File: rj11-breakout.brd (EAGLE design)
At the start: 100 x 80 mm, 2 parts, among them J1 22-27-2061-06, X1 XRJK-S-01-6-6-0-2G2-NO

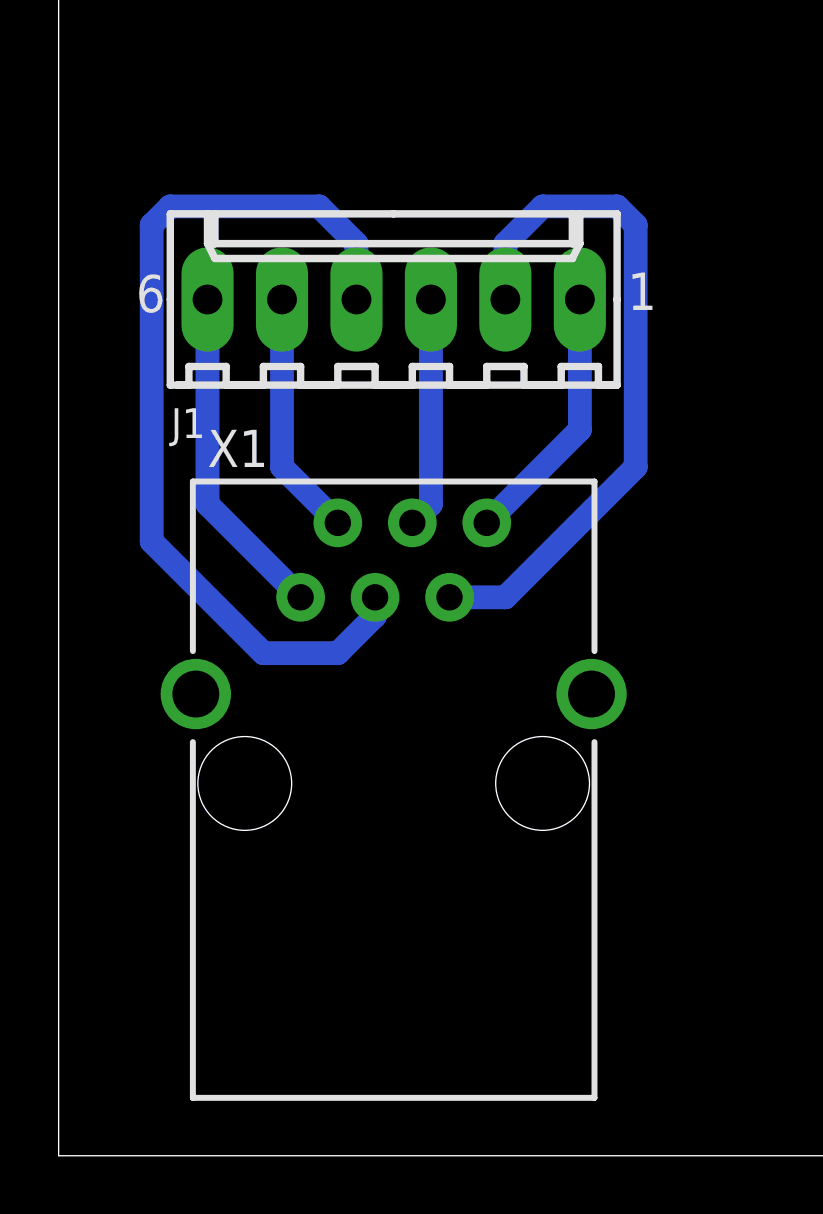
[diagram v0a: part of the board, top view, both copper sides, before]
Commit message: changed to correct RJ11 part
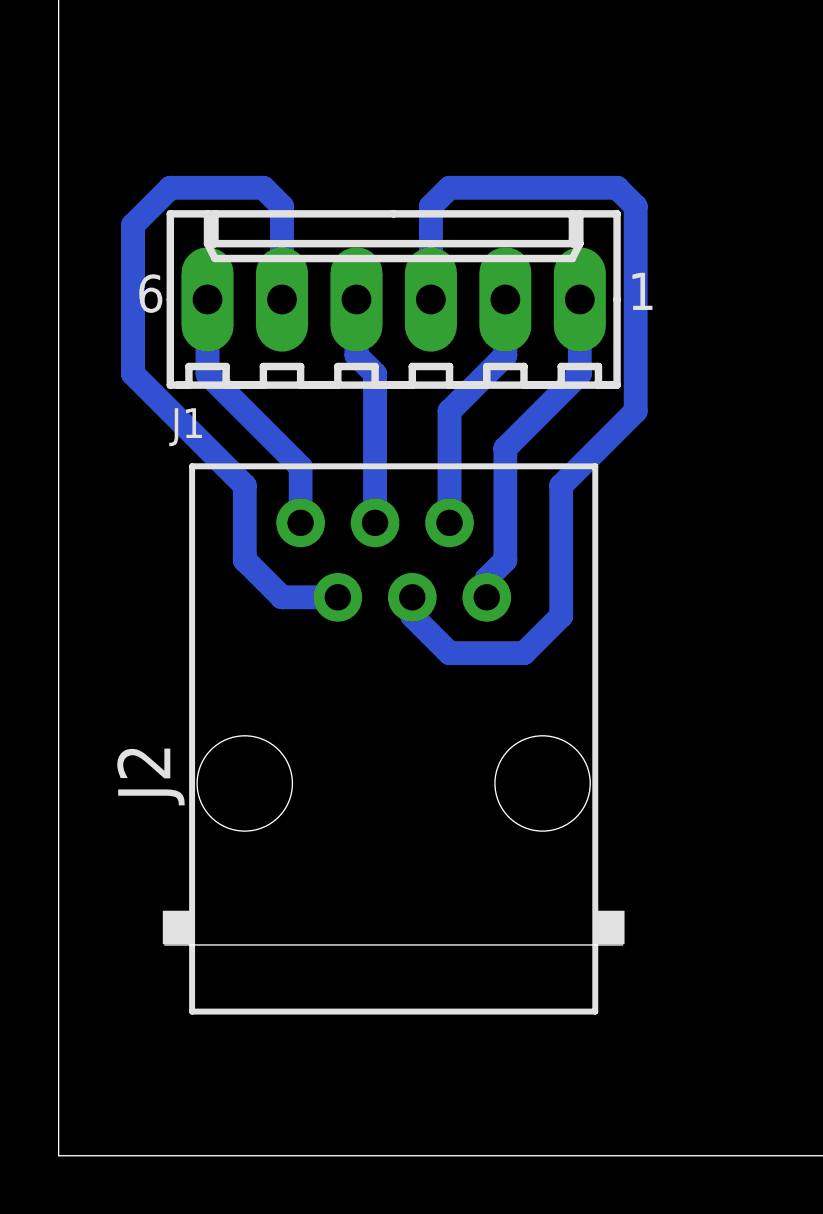
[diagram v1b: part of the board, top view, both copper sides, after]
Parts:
- removed X1: XRJK-S-01-6-6-0-2G2-NO, con-xmultiple:XRJK-S-01-6-6-0-2G2-NO
- added J2: RJ11-6L-B, con-tycoelectronics:RJ11-NO_SHIELD
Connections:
- net N$1: now also J1.1, J2.6; no longer J1.6, X1.1
- net N$2: now also J1.2, J2.5; no longer J1.5, X1.2
- net N$3: now also J1.3, J2.4; no longer J1.4, X1.3
- net N$4: now also J1.4, J2.3; no longer J1.3, X1.4
- net N$5: now also J1.5, J2.2; no longer J1.2, X1.5
- net N$6: now also J1.6, J2.1; no longer J1.1, X1.6
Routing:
- net N$5: track 23.6 -> 25.8 mm
- net N$3: track 30.8 -> 32.5 mm
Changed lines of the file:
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@@
 </autorouter>
 <elements>
-<element name="X1" library="con-xmultiple" package="XRJK-S-01-6-6-0-2G2-NO" value="XRJK-S-01-6-6-0-2G2-NO" x="11.43" y="12.7"/>
 <element name="J1" library="con-molex" package="6410-06" value="22-27-2061-06" x="11.43" y="29.21">
 <attribute name="OC_NEWARK" value="unknown" x="34.29" y="0" size="1.778" layer="27" display="off"/>
@@
 <attribute name="OC_FARNELL" value="unknown" x="34.29" y="0" size="1.778" layer="27" display="off"/>
 </element>
+<element name="J2" library="con-tycoelectronics" package="RJ11-NO_SHIELD" value="RJ11-6L-B" x="11.43" y="12.7">
+<attribute name="OC_NEWARK" value="52K3613" x="11.43" y="12.7" size="1.778" layer="27" display="off"/>
+<attribute name="MPN" value="RJ11-6L-B" x="11.43" y="12.7" size="1.778" layer="27" display="off"/>
+<attribute name="MF" value="TYCO ELECTRONICS" x="11.43" y="12.7" size="1.778" layer="27" display="off"/>
+<attribute name="OC_FARNELL" value="unknown" x="11.43" y="12.7" size="1.778" layer="27" display="off"/>
+</element>
 </elements>
 <signals>
 <signal name="N$1">
-<contactref element="X1" pad="1"/>
-<contactref element="J1" pad="6"/>
-<wire x1="5.08" y1="29.21" x2="5.08" y2="22.225" width="0.8128" layer="16"/>
-<wire x1="5.08" y1="22.225" x2="8.255" y2="19.05" width="0.8128" layer="16"/>
+<contactref element="J1" pad="1"/>
+<contactref element="J2" pad="6"/>
+<wire x1="14.605" y1="19.05" x2="14.605" y2="19.685" width="0.8128" layer="16"/>
+<wire x1="14.605" y1="19.685" x2="15.24" y2="20.32" width="0.8128" layer="16"/>
+<wire x1="15.24" y1="20.32" x2="15.24" y2="24.13" width="0.8128" layer="16"/>
+<wire x1="15.24" y1="24.13" x2="17.78" y2="26.67" width="0.8128" layer="16"/>
+<wire x1="17.78" y1="26.67" x2="17.78" y2="29.21" width="0.8128" layer="16"/>
 </signal>
 <signal name="N$2">
-<contactref element="X1" pad="2"/>
-<contactref element="J1" pad="5"/>
-<wire x1="7.62" y1="29.21" x2="7.62" y2="23.495" width="0.8128" layer="16"/>
-<wire x1="7.62" y1="23.495" x2="9.525" y2="21.59" width="0.8128" layer="16"/>
+<contactref element="J1" pad="2"/>
+<contactref element="J2" pad="5"/>
+<wire x1="13.335" y1="21.59" x2="13.335" y2="25.4" width="0.8128" layer="16"/>
+<wire x1="13.335" y1="25.4" x2="15.24" y2="27.305" width="0.8128" layer="16"/>
+<wire x1="15.24" y1="27.305" x2="15.24" y2="29.21" width="0.8128" layer="16"/>
 </signal>
 <signal name="N$3">
-<contactref element="X1" pad="3"/>
-<contactref element="J1" pad="4"/>
-<wire x1="10.795" y1="19.05" x2="10.795" y2="18.415" width="0.8128" layer="16"/>
-<wire x1="10.795" y1="18.415" x2="9.525" y2="17.145" width="0.8128" layer="16"/>
-<wire x1="9.525" y1="17.145" x2="6.985" y2="17.145" width="0.8128" layer="16"/>
-<wire x1="6.985" y1="17.145" x2="3.175" y2="20.955" width="0.8128" layer="16"/>
-<wire x1="3.175" y1="20.955" x2="3.175" y2="31.75" width="0.8128" layer="16"/>
-<wire x1="3.175" y1="31.75" x2="3.81" y2="32.385" width="0.8128" layer="16"/>
-<wire x1="3.81" y1="32.385" x2="8.89" y2="32.385" width="0.8128" layer="16"/>
-<wire x1="8.89" y1="32.385" x2="10.16" y2="31.115" width="0.8128" layer="16"/>
-<wire x1="10.16" y1="31.115" x2="10.16" y2="29.21" width="0.8128" layer="16"/>
+<contactref element="J1" pad="3"/>
+<contactref element="J2" pad="4"/>
+<wire x1="12.065" y1="19.05" x2="12.065" y2="18.415" width="0.8128" layer="16"/>
+<wire x1="12.065" y1="18.415" x2="13.335" y2="17.145" width="0.8128" layer="16"/>
+<wire x1="13.335" y1="17.145" x2="15.875" y2="17.145" width="0.8128" layer="16"/>
+<wire x1="15.875" y1="17.145" x2="17.145" y2="18.415" width="0.8128" layer="16"/>
+<wire x1="17.145" y1="18.415" x2="17.145" y2="22.86" width="0.8128" layer="16"/>
+<wire x1="17.145" y1="22.86" x2="19.685" y2="25.4" width="0.8128" layer="16"/>
+<wire x1="19.685" y1="25.4" x2="19.685" y2="32.385" width="0.8128" layer="16"/>
+<wire x1="19.685" y1="32.385" x2="19.05" y2="33.02" width="0.8128" layer="16"/>
+<wire x1="19.05" y1="33.02" x2="13.335" y2="33.02" width="0.8128" layer="16"/>
+<wire x1="13.335" y1="33.02" x2="12.7" y2="32.385" width="0.8128" layer="16"/>
+<wire x1="12.7" y1="32.385" x2="12.7" y2="29.21" width="0.8128" layer="16"/>
 </signal>
 <signal name="N$4">
-<contactref element="X1" pad="4"/>
-<contactref element="J1" pad="3"/>
-<wire x1="12.7" y1="29.21" x2="12.7" y2="22.225" width="0.8128" layer="16"/>
-<wire x1="12.7" y1="22.225" x2="12.065" y2="21.59" width="0.8128" layer="16"/>
+<contactref element="J1" pad="4"/>
+<contactref element="J2" pad="3"/>
+<wire x1="10.16" y1="29.21" x2="10.16" y2="27.305" width="0.8128" layer="16"/>
+<wire x1="10.16" y1="27.305" x2="10.795" y2="26.67" width="0.8128" layer="16"/>
+<wire x1="10.795" y1="26.67" x2="10.795" y2="21.59" width="0.8128" layer="16"/>
 </signal>
 <signal name="N$5">
-<contactref element="X1" pad="5"/>
-<contactref element="J1" pad="2"/>
-<wire x1="13.335" y1="19.05" x2="15.24" y2="19.05" width="0.8128" layer="16"/>
-<wire x1="15.24" y1="19.05" x2="19.685" y2="23.495" width="0.8128" layer="16"/>
-<wire x1="19.685" y1="23.495" x2="19.685" y2="31.75" width="0.8128" layer="16"/>
-<wire x1="19.685" y1="31.75" x2="19.05" y2="32.385" width="0.8128" layer="16"/>
-<wire x1="19.05" y1="32.385" x2="16.51" y2="32.385" width="0.8128" layer="16"/>
-<wire x1="16.51" y1="32.385" x2="15.24" y2="31.115" width="0.8128" layer="16"/>
-<wire x1="15.24" y1="31.115" x2="15.24" y2="29.21" width="0.8128" layer="16"/>
+<contactref element="J1" pad="5"/>
+<contactref element="J2" pad="2"/>
+<wire x1="9.525" y1="19.05" x2="7.62" y2="19.05" width="0.8128" layer="16"/>
+<wire x1="7.62" y1="19.05" x2="6.35" y2="20.32" width="0.8128" layer="16"/>
+<wire x1="6.35" y1="20.32" x2="6.35" y2="22.86" width="0.8128" layer="16"/>
+<wire x1="6.35" y1="22.86" x2="2.54" y2="26.67" width="0.8128" layer="16"/>
+<wire x1="2.54" y1="26.67" x2="2.54" y2="31.75" width="0.8128" layer="16"/>
+<wire x1="2.54" y1="31.75" x2="3.81" y2="33.02" width="0.8128" layer="16"/>
+<wire x1="3.81" y1="33.02" x2="6.985" y2="33.02" width="0.8128" layer="16"/>
+<wire x1="6.985" y1="33.02" x2="7.62" y2="32.385" width="0.8128" layer="16"/>
+<wire x1="7.62" y1="32.385" x2="7.62" y2="29.21" width="0.8128" layer="16"/>
 </signal>
 <signal name="N$6">
-<contactref element="X1" pad="6"/>
-<contactref element="J1" pad="1"/>
-<wire x1="17.78" y1="29.21" x2="17.78" y2="24.765" width="0.8128" layer="16"/>
-<wire x1="17.78" y1="24.765" x2="14.605" y2="21.59" width="0.8128" layer="16"/>
+<contactref element="J1" pad="6"/>
+<contactref element="J2" pad="1"/>
+<wire x1="8.255" y1="21.59" x2="8.255" y2="23.495" width="0.8128" layer="16"/>
+<wire x1="8.255" y1="23.495" x2="5.08" y2="26.67" width="0.8128" layer="16"/>
+<wire x1="5.08" y1="26.67" x2="5.08" y2="29.21" width="0.8128" layer="16"/>
 </signal>
 </signals>
